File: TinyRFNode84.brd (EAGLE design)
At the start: 32 x 42.6 mm, 14 parts, among them IC3 MCP1703CB, T1 2N2222, U1 ATTINY84-20SSU

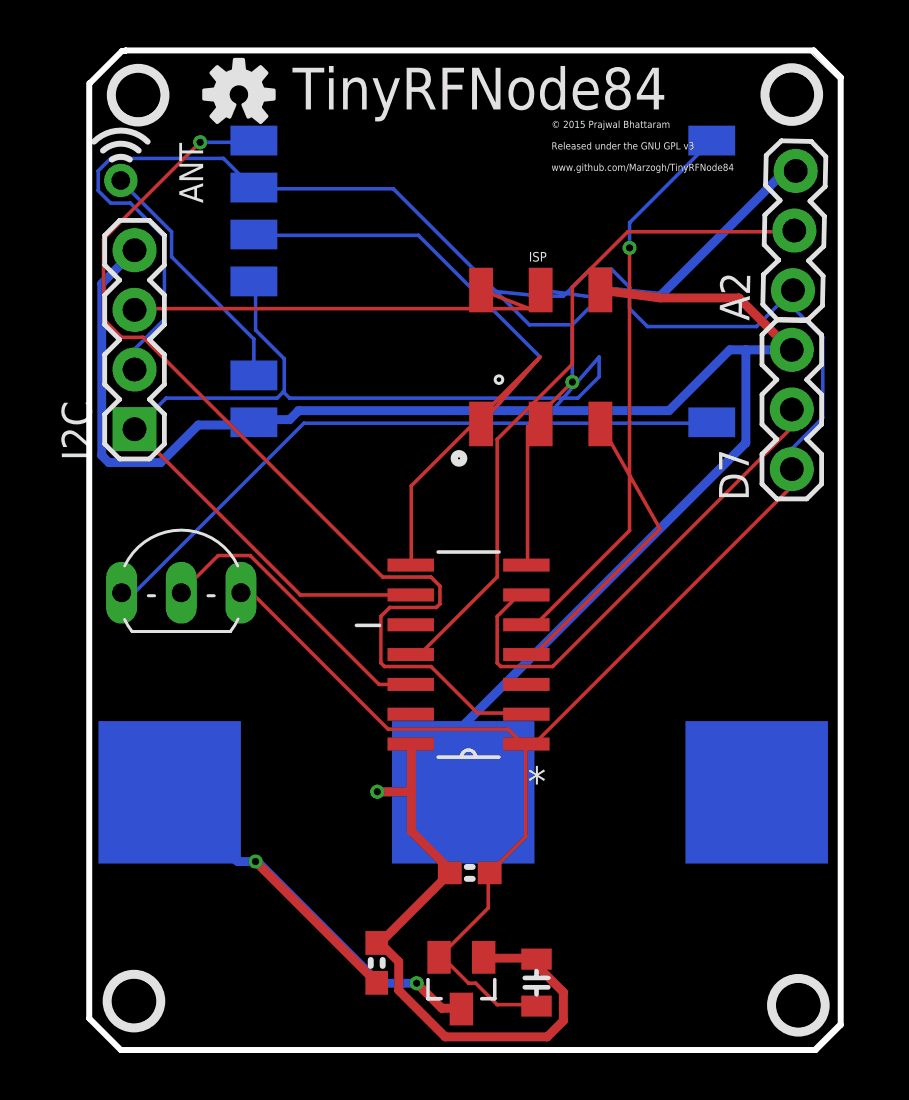
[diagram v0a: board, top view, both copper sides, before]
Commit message: Fixed a few routing errors
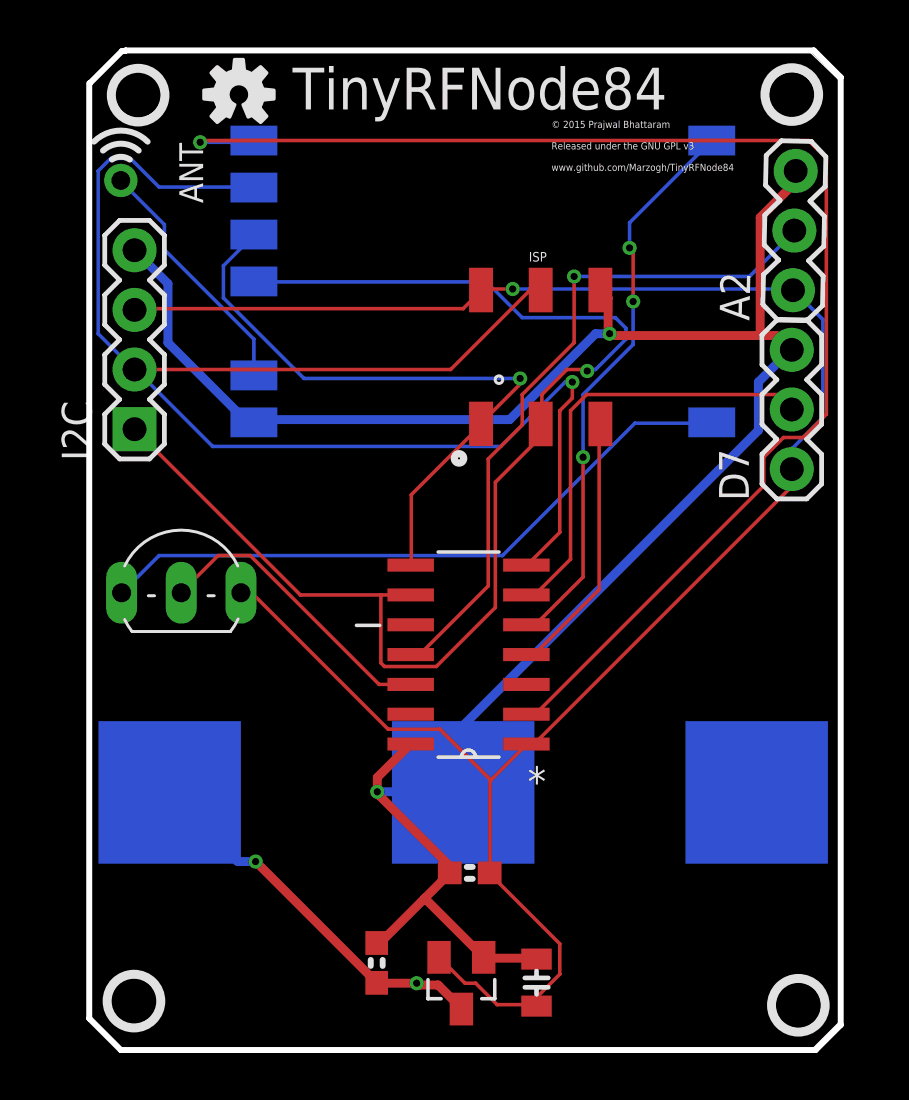
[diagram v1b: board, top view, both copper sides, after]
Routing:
- net GND: track 115.9 -> 89.9 mm, vias 1 -> 2
- net SS: track 43.2 -> 59.1 mm
- net MOSI/SDA: track 49.2 -> 64.9 mm
- net SCK/SCL: track 45.5 -> 55.2 mm, vias 0 -> 1
- net PWR: track 23.6 -> 16.3 mm
- net MISO: track 33.1 -> 27.2 mm, vias 0 -> 1
- net VCC: track 91.1 -> 86.2 mm, vias 0 -> 1
- net D7: track 21.2 -> 18.8 mm
- net RST: track 13.0 -> 11.3 mm
- net D2: track 29.2 -> 29.4 mm, vias 0 -> 1
- net D8: track 24.1 -> 24.2 mm, vias 1 -> 3

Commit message: v2.0.2
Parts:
- removed A2, D7: (no value), SparkFun-Connectors:1X03
- removed I2C: (no value), SparkFun-Connectors:1X04
- removed ISP: (no value), SparkFun-Connectors:2X3_SMD
- removed T1: 2N2222, adafruit:TO92-EBC-OVAL
- added D1: RED, SparkFun-LED:LED-0603
- added D2: GREEN, SparkFun-LED:LED-0603
- added D3, D4: MBRA140, SparkFun-DiscreteSemi:SMA-DIODE
- added ICSP: ICSP, SparkFun-Connectors:1X06_NO_SILK
- added JP1: M09, SparkFun-Connectors:1X09
- added JP2, JP3: M02PTH, SparkFun-Connectors:1X02
- added Q1: MOSFET-NCHANNELBSS138, SparkFun-DiscreteSemi:SOT23
- added R1, R2: 220, SparkFun-Passives:0603-RES
- added R3: 4k7, SparkFun-Passives:0402-RES
- added S1: RESET, SparkFun-Electromechanical:TACTILE-SWITCH-SMD
- added U$3: (no value), SparkFun-Aesthetics:OSHW-LOGO-S
- BAT1: device SparkFun-Electromechanical:BATTCON_20MM -> SparkFun-Electromechanical:BATTCON_12MM
- moved U$1 27.5 mm to (29.1, 34.3)
- moved U$2 23.2 mm to (29.1, 34.3), flipped to the bottom
- moved C3 22.1 mm to (30.2, 22.1), turned to 0 degrees
- moved IC3 19.2 mm to (30.4, 15.8), flipped to the bottom
- moved C2 19.0 mm to (27.6, 15.3), flipped to the bottom
- moved C4 18.2 mm to (30.0, 19.8), turned to 0 degrees
- moved U$5 13.5 mm to (18.5, 20.5), turned to 90 degrees
- moved U1 7.97 mm to (17.9, 24.7)
- moved BAT1 3.35 mm to (19.0, 13.0), flipped to the top
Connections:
- net D8 renamed D8/INT0
- removed net AREF: U1.13
- removed net D1: T1.B, U1.12
- removed net D2: A2.2, U1.11
- removed net D3: U1.10
- removed net D7: D7.2, U1.6
- removed net SS: U$5.NSS, U1.2
- removed net VDD: T1.E, U$5.VDD
- new net 3V: C2.1, D3.C, D4.C, IC3.3
- new net BAT: BAT1.PWR@1, D3.A
- new net D0/A0/AREF: JP1.9, U1.13
- new net D1/A1: JP1.8, Q1.1, U1.12
- new net D10/SS: R1.2, U$5.NSS, U1.2
- new net D2/A2: JP1.7, U1.11
- new net D3/A3: JP1.6, U1.10
- new net D7/A7: JP1.2, U1.6
- new net N$12: D1.A, R2.1
- new net N$13: D2.A, R1.1
- new net SW_GND: D1.C, D2.C, JP3.1, Q1.2, U$5.GND
- net D9: now also JP1.1, R2.2
- net GND: now also BAT1.GND, ICSP.5, JP2.1, Q1.3, S1.1; no longer A2.3, BAT1.2, D7.3, I2C.4, ISP.6, U$5.GND
- net MISO: now also ICSP.3, JP1.4; no longer ISP.1
- net MOSI/SDA: now also ICSP.6, JP1.3; no longer I2C.2, ISP.4
- net PWR: now also D4.A, JP2.2; no longer BAT1.1, C2.1, IC3.3
- net RST: now also ICSP.1, R3.1, S1.3; no longer ISP.5
- net SCK/SCL: now also ICSP.2, JP1.5; no longer I2C.1, ISP.3
- net VCC: now also ICSP.4, JP3.2, R3.2, U$5.VDD; no longer A2.1, D7.1, I2C.3, ISP.2, T1.C
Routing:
- net SS: track 59.1 -> 0.00 mm, vias 1 -> 0
- net SW_GND: track 0.00 -> 43.3 mm, vias 0 -> 3
- net RST: track 11.3 -> 51.4 mm, vias 0 -> 1
- net MOSI/SDA: track 64.9 -> 35.0 mm
- net D2: track 29.4 -> 0.00 mm, vias 1 -> 0
- net VDD: track 28.1 -> 0.00 mm
- net SCK/SCL: track 55.2 -> 27.7 mm, vias 1 -> 2
- net D9: track 0.00 -> 25.8 mm
- net 3V: track 0.00 -> 20.2 mm, vias 0 -> 1
- net D7: track 18.8 -> 0.00 mm
- net D7/A7: track 0.00 -> 15.3 mm
- net D0/A0/AREF: track 0.00 -> 13.9 mm
- net D1/A1: track 0.00 -> 12.7 mm
- net D1: track 12.7 -> 0.00 mm
- net D2/A2: track 0.00 -> 11.8 mm, vias 0 -> 1
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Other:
- board size 32 x 42.6 mm -> 28.9 x 35.1 mm
- board text added: "3.3V"
- board text added: "A0/D0"
- board text added: "A1/D1"
- board text added: "A2/D2"
- board text added: "A3/D3"
- board text added: "A4/D4"
- board text added: "A5/D5"
- board text added: "A6/D6"
- board text added: "A7/D7"
- board text added: "Ant"
- board text added: "D9"
- board text added: "Ext. 3.3V"
- board text added: "GND"
- board text added: "GND {Switched}"
- board text added: "MISO"
- board text added: "MOSI"
- board text added: "RST"
- board text added: "SCK"
- board text added: "VCC"
- board text added: "© GNU GPL v3 2015 Prajwal Bhattaram www.github.com/Marzogh/TinyRFNode84"
- board text removed: "ANT"
- board text removed: "© 2015 Prajwal Bhattaram Released under the GNU GPL v3 www.github.com/Marzogh/TinyRFNode84"
